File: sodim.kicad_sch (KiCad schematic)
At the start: 1 part, among them J1 Bus_DDR4_Edge_Conn

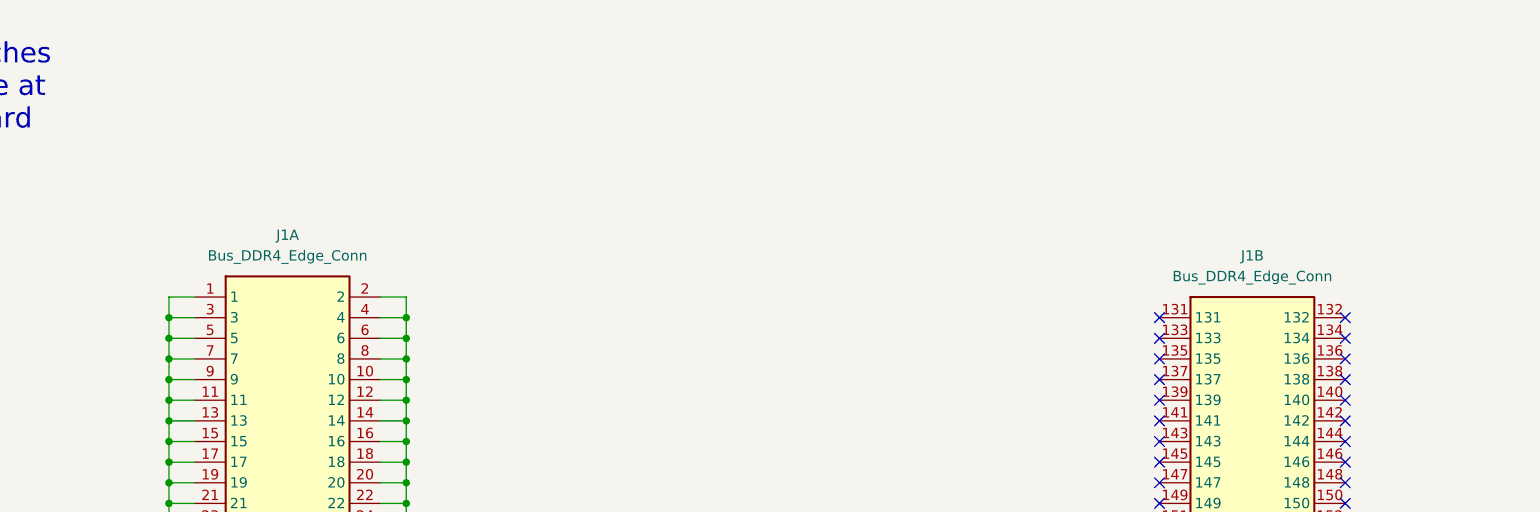
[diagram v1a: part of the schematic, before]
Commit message: Update edge connector on schematic
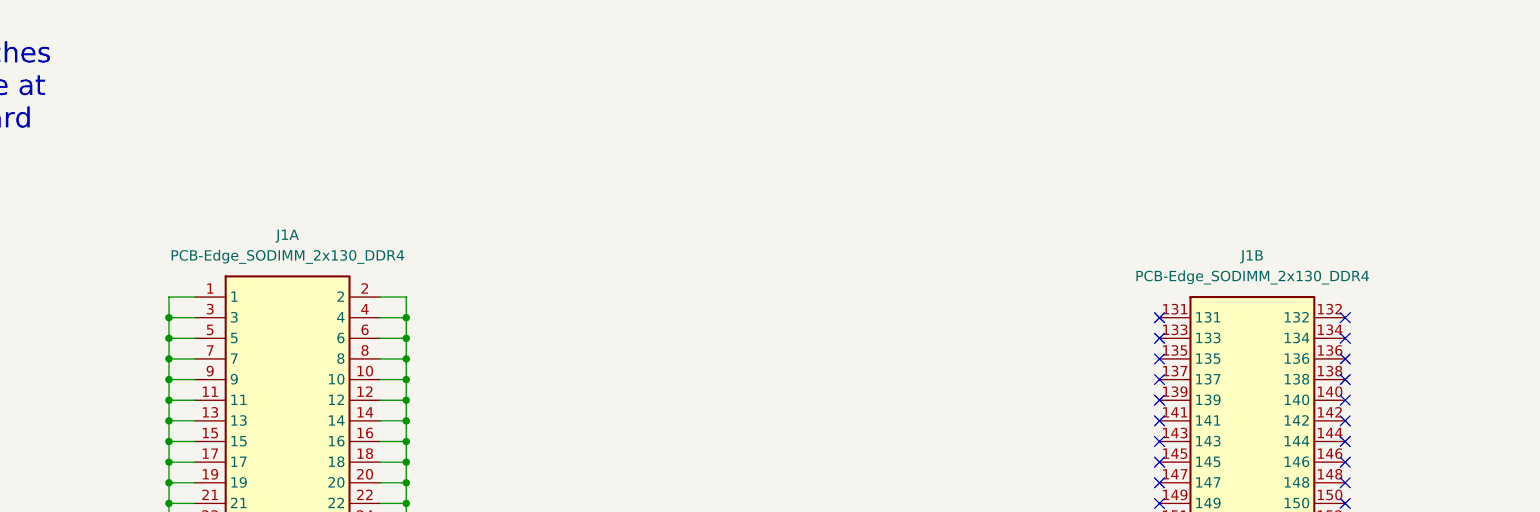
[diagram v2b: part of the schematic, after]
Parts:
- removed J1: Bus_DDR4_Edge_Conn, ddr5-testbed-footprints:Bus_DDR4_Conn_Edge, symbol ddr5-testbed:Bus_DDR4_Edge_Conn
- added J1: PCB-Edge_SODIMM_2x130_DDR4, antmicro-footprints:PCB-Edge_SODIMM_2x130_DDR4, symbol antmicroEdgeConnectors:PCB-Edge_SODIMM_2x130_DDR4
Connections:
- net 1V1_SYS: now also J1.101, J1.103, J1.105, J1.107, J1.93, J1.95, J1.97, J1.99
- net 1V8_SYS: now also J1.116, J1.118, J1.120, J1.122, J1.124
- net ALERT_N: now also J1.158
- net CA0: now also J1.181
- net CA1: now also J1.197
- net CA10: now also J1.165
- net CA11: now also J1.183
- net CA12: now also J1.163
- net CA13: now also J1.185
- net CA2: now also J1.171
- net CA3: now also J1.191
- net CA4: now also J1.179
- net CA5: now also J1.193
- net CA6: now also J1.169
- net CA7: now also J1.189
- net CA8: now also J1.167
- net CA9: now also J1.187
- net CAI: now also J1.156
- net CLK_N: now also J1.173
- net CLK_P: now also J1.175
- net CS_N: now also J1.162
- net DQ0: now also J1.198
- net DQ1: now also J1.192
- net DQ2: now also J1.196
- net DQ3: now also J1.194
- net DQ4: now also J1.186
- net DQ5: now also J1.180
- net DQ6: now also J1.178
- net DQ7: now also J1.182
- net DQS_N: now also J1.199
- net DQS_P: now also J1.201
- net GND: now also J1.1, J1.10, J1.11, J1.12, J1.13, J1.14, J1.15, J1.154, J1.16, J1.161, J1.168, J1.17, J1.177, J1.18, J1.184, J1.19, J1.195, J1.2, J1.20, J1.200, J1.21, J1.210, J1.211, J1.22, J1.23, J1.24, J1.25, J1.26, J1.27, J1.28, J1.29, J1.3, J1.30, J1.31, J1.32, J1.33, J1.34, J1.35, J1.36, J1.37, J1.38, J1.39, J1.4, J1.40, J1.41, J1.42, J1.43, J1.44, J1.45, J1.46, J1.47, J1.48, J1.49, J1.5, J1.50, J1.6, J1.7, J1.8, J1.9
- net LBDQ: now also J1.209
- net LBDQS: now also J1.207
- net MIR: now also J1.160
- net OTD_CA_A: now also J1.206
- net RESET_N: now also J1.203
- net SCL: now also J1.129
- net SDA: now also J1.127
- net TDQS_N: now also J1.164
- net TDQS_P: now also J1.166
- net TEN: now also J1.205
